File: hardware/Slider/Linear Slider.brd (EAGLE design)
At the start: 89.4 x 17.5 mm, 9 parts

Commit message: Updates
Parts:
- moved R2 5.75 mm to (78.2, 12.7)
- moved R3 5.23 mm to (23.4, 11.2), turned to 135 degrees
- moved C1 5.08 mm to (65.8, 8.38)
- moved LD1 5.08 mm to (86.9, 6.10)
- moved R1 5.08 mm to (81.8, 4.57)
- moved R4 5.08 mm to (16.8, 8.13)
- moved LD2 5.08 mm to (2.79, 6.10)
- moved POT1 5.08 mm to (44.8, 6.10)
- moved SERIAL 5.08 mm to (66.8, 13.7)
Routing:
- net SLIDER_IN: track 63.0 -> 65.5 mm
- net LED_TOP_G: track 11.5 -> 10.2 mm
- net N$4: track 23.8 -> 22.9 mm
- net LED_BOT_R: track 38.4 -> 39.3 mm
- net N$2: track 12.5 -> 13.1 mm
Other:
- board size 89.4 x 17.5 mm -> 89.4 x 16.5 mm
- board text added: "peschuster.de - 05/2013"

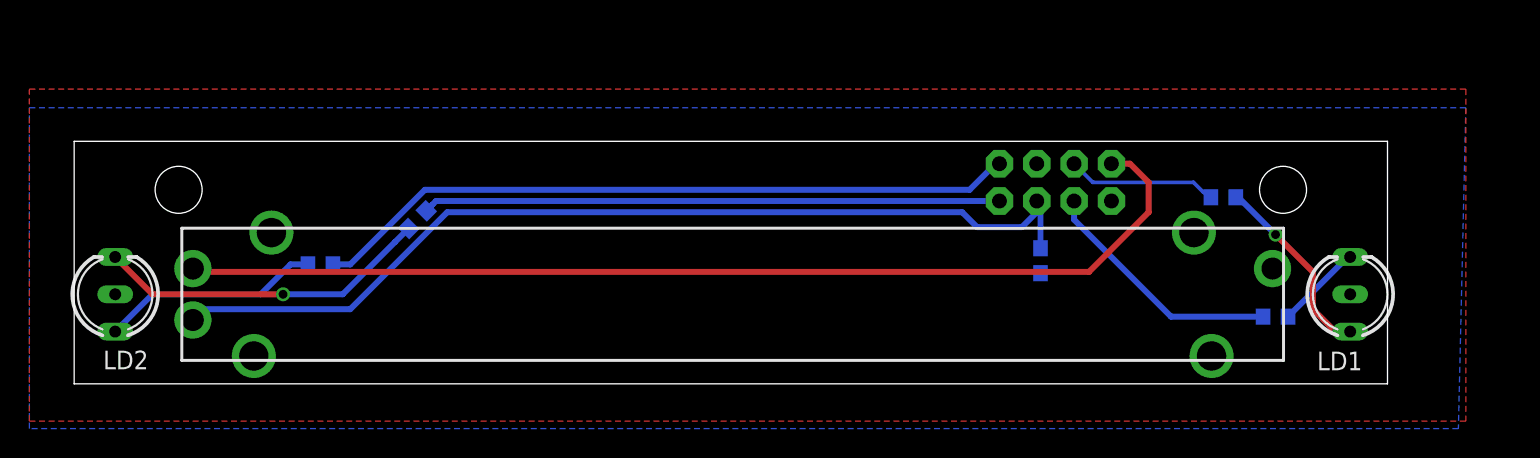
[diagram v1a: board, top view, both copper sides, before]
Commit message: Ordered Version
Small mechanical changes
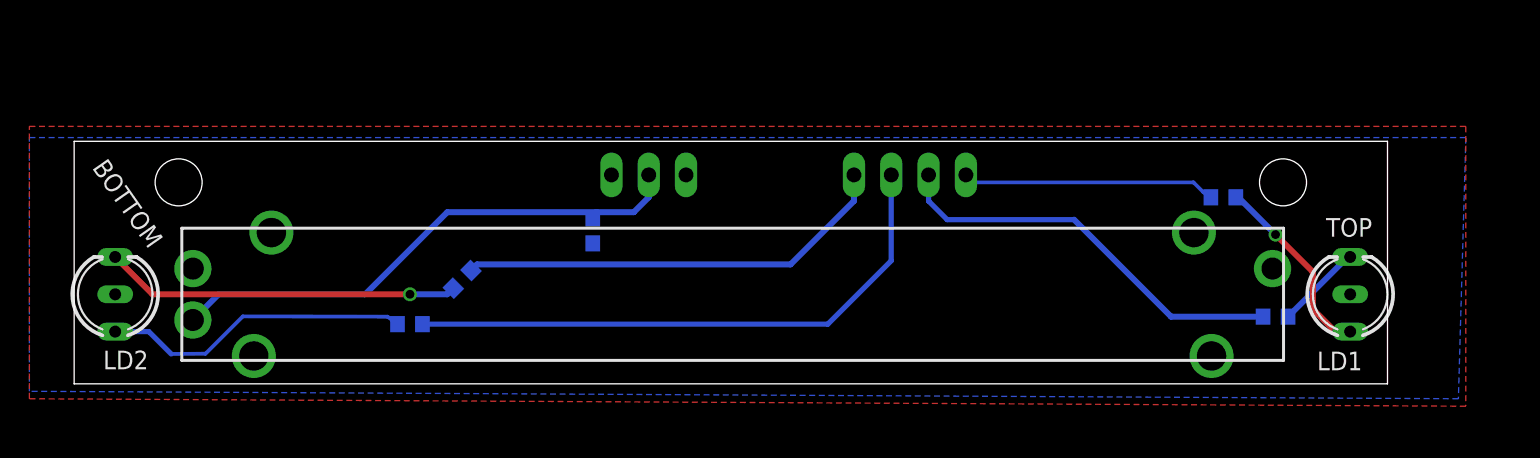
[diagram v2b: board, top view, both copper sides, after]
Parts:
- removed SERIAL: M04X2, SparkFun:2X4
- added LEDS: (no value), con-lstb:MA04-1
- added SLIDER: (no value), con-lstb:MA03-1
- moved C1 30.5 mm to (35.3, 10.4)
- moved R4 7.33 mm to (22.9, 4.06)
- moved R3 5.08 mm to (26.4, 7.11)
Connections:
- net 5V: no longer SERIAL.2
- net GND: no longer SERIAL.1
- net LED_BOT_G: now also LEDS.2; no longer SERIAL.8
- net LED_BOT_R: now also LEDS.1; no longer SERIAL.7
- net LED_TOP_G: now also LEDS.4; no longer SERIAL.4
- net LED_TOP_R: now also LEDS.3; no longer SERIAL.3
- net SLIDER_IN: now also SLIDER.2; no longer SERIAL.5
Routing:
- net 5V: track 71.9 -> 0.65 mm
- net SLIDER_IN: track 65.5 -> 36.5 mm
- net LED_TOP_R: track 16.9 -> 27.8 mm
- net LED_BOT_R: track 39.3 -> 29.8 mm
- net LED_BOT_G: track 48.2 -> 39.5 mm
- net LED_TOP_G: track 10.2 -> 17.3 mm
- net N$3: track 15.0 -> 21.1 mm
- net N$4: track 22.9 -> 24.2 mm
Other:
- board text removed: "1"
- board text removed: "8"

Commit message: New version of slider board
Common anode, molex conn. (ordered)
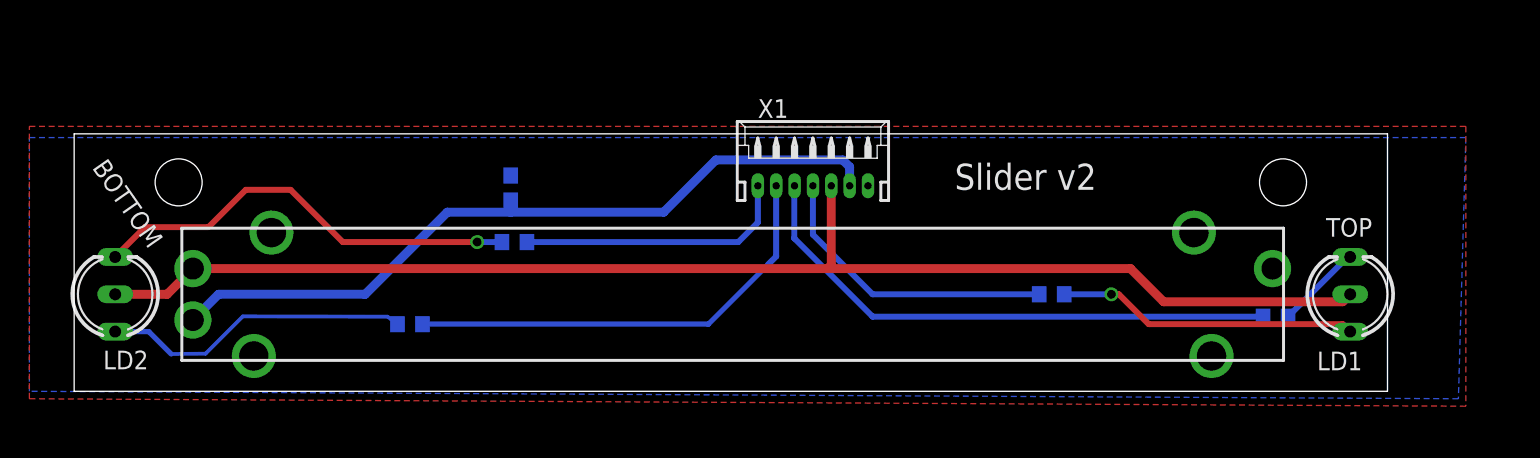
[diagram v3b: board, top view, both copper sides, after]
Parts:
- removed LEDS: (no value), con-lstb:MA04-1
- removed SLIDER: (no value), con-lstb:MA03-1
- added X1: 53048-07, con-molex:53048-07
- LD1, LD2: device led:DUOLED-C-5MM -> led:DUOLED-A-5MM
- moved R2 13.4 mm to (66.5, 6.10)
- moved C1 6.30 mm to (29.7, 13.3), turned to 90 degrees
- moved R3 4.37 mm to (30.0, 9.65), turned to 180 degrees
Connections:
- net 5V: now also LD1.A, LD2.A, X1.3
- net GND: now also X1.1; no longer LD1.C, LD2.C
- net LED_BOT_G: now also X1.6; no longer LEDS.2
- net LED_BOT_R: now also X1.7; no longer LEDS.1
- net LED_TOP_G: now also X1.4; no longer LEDS.4
- net LED_TOP_R: now also X1.5; no longer LEDS.3
- net N$1: now also LD1.CR; no longer LD1.AR
- net N$2: now also LD1.CX; no longer LD1.AX
- net N$3: now also LD2.CX; no longer LD2.AX
- net N$4: now also LD2.CR; no longer LD2.AR
- net SLIDER_IN: now also X1.2; no longer SLIDER.2
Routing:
- net 5V: track 0.65 -> 91.7 mm
- net SLIDER_IN: track 36.5 -> 51.5 mm
- net LED_BOT_R: track 29.8 -> 18.8 mm
- net LED_TOP_R: track 27.8 -> 37.7 mm
- net LED_BOT_G: track 39.5 -> 31.2 mm
- net N$2: track 13.1 -> 20.5 mm
- net N$4: track 24.2 -> 29.7 mm
- net LED_TOP_G: track 17.3 -> 20.4 mm
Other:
- board size 89.4 x 16.5 mm -> 89.4 x 17.5 mm
- board text added: "Slider v2"
- board text added: "peschuster.de - 01/2015"
- board text removed: "peschuster.de - 05/2013"
